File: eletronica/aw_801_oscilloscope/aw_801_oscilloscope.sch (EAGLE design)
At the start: 54 parts, among them IC1 ICL7660CPA, IC3 MEGA8-P, IC4 LM4558N, Q2 16Mhz, X1 ANALOG, X2 USB, X3 DIG

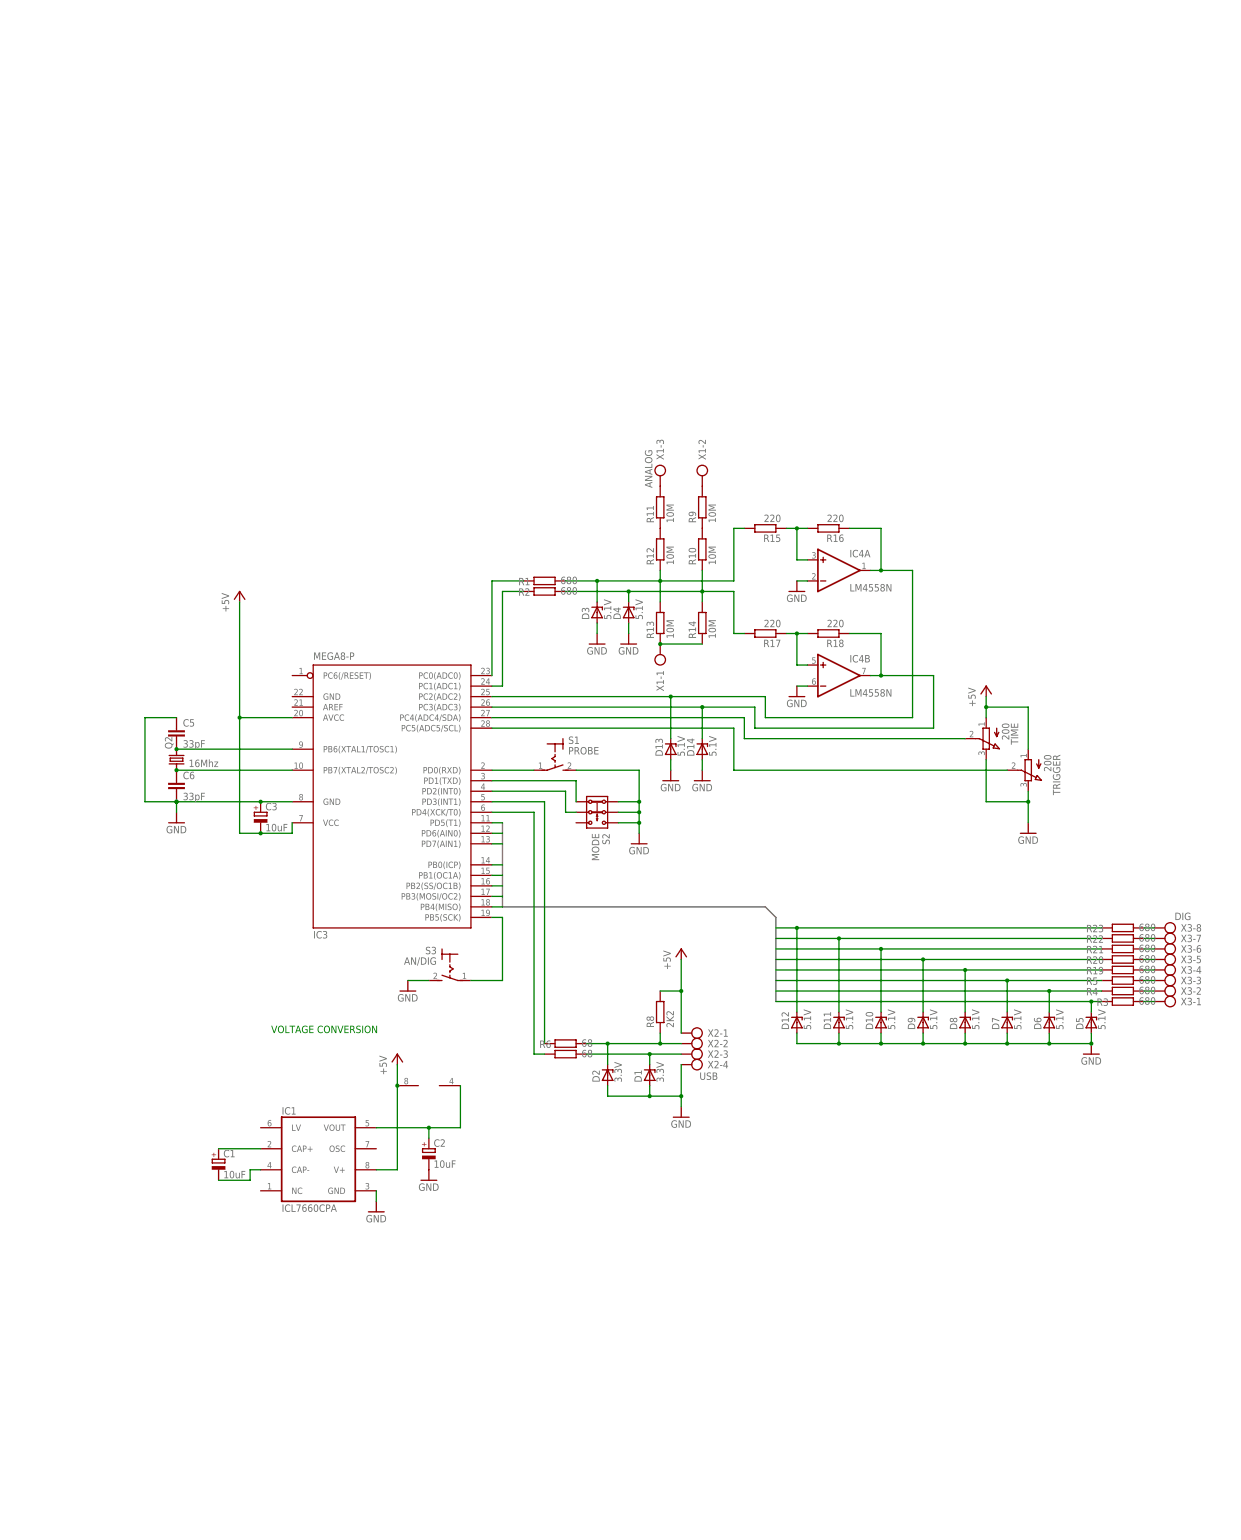
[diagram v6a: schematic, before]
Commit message: 
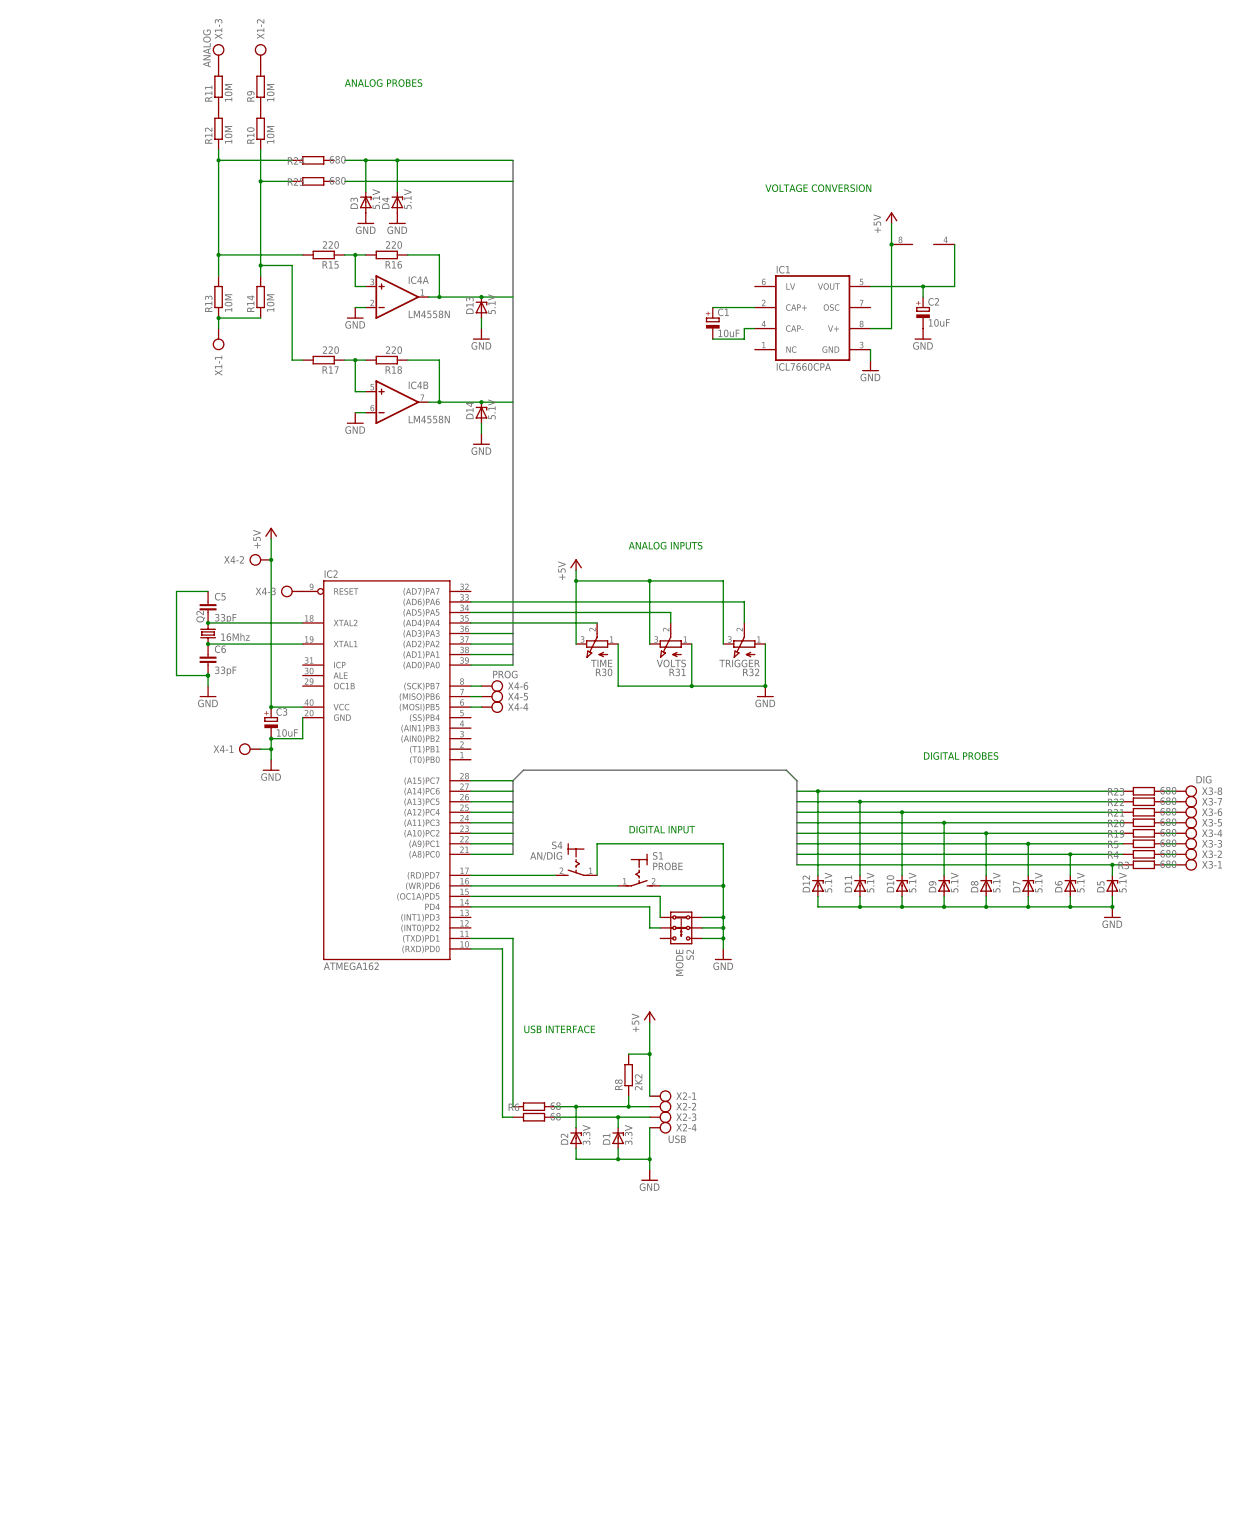
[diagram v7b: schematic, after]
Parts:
- removed IC3: MEGA8-P, atmel:MEGA8-P
- removed R1, R2: 680, rcl:R-EU_0207/10
- removed S3: AN/DIG, switch:MS243
- removed TIME, TRIGGER: 200, pot:3RP/1610N
- added IC2: ATMEGA162, atmel:AT90S8515P
- added R24, R25: 680, rcl:R-EU_0207/10
- added R30: TIME, pot:3RP/1610N
- added R31: VOLTS, pot:3RP/1610N
- added R32: TRIGGER, pot:3RP/1610N
- added S4: AN/DIG, switch:MS243
- added X4: PROG, con-ptr500:AK300/6
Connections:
- removed net N$35: IC3.PB5(SCK), S3.P
- new net ANALOG0: D3.C, D4.C, IC2.(AD0)PA0
- new net ANALOG1: IC2.(AD1)PA1
- new net ANALOG2: D13.C, IC2.(AD2)PA2, IC4A.OUT, R16.1
- new net ANALOG3: D14.C, IC2.(AD3)PA3, IC4B.OUT, R18.1
- new net N$36: IC2.(WR)PD6, S1.P
- new net N$37: IC2.(TXD)PD1, R6.1
- net +5V: now also C3.+, IC2.VCC, R30.E, R31.E, R32.E, X4-2.KL; no longer C3.-, IC3.AVCC, IC3.VCC@1, TIME.A, TRIGGER.A
- net DIG0: now also IC2.(A8)PC0; no longer IC3.PD5(T1)
- net DIG1: now also IC2.(A9)PC1; no longer IC3.PD6(AIN0)
- net DIG2: now also IC2.(A10)PC2; no longer IC3.PD7(AIN1)
- net DIG3: now also IC2.(A11)PC3; no longer IC3.PB0(ICP)
- net DIG4: now also IC2.(A12)PC4; no longer IC3.PB1(OC1A)
- net DIG5: now also IC2.(A13)PC5; no longer IC3.PB2(SS/OC1B)
- net DIG6: now also IC2.(A14)PC6; no longer IC3.PB3(MOSI/OC2)
- net DIG7: now also IC2.(A15)PC7; no longer IC3.PB4(MISO)
- net GND: now also C3.-, IC2.GND, R30.A, R31.A, R32.A, S4.P, X4-1.KL; no longer C3.+, IC3.GND@1, S3.S, TIME.E, TRIGGER.E
- net N$1: now also R24.1; no longer D3.C, R1.2
- net N$11: now also IC2.(SCK)PB7, X4-6.KL; no longer IC3.PD3(INT1), R6.1
- net N$12: now also IC2.(RXD)PD0; no longer IC3.PD4(XCK/T0)
- net N$16: now also R25.1; no longer D4.C, R2.2
- net N$18: now also IC2.(AD5)PA5, R31.S; no longer D13.C, IC3.PC2(ADC2), IC4A.OUT, R16.1
- net N$20: now also IC2.(AD6)PA6, R32.S; no longer D14.C, IC3.PC3(ADC3), IC4B.OUT, R18.1
- net N$22: now also IC2.(MISO)PB6, X4-5.KL; no longer IC3.PC4(ADC4/SDA), TIME.S
- net N$23: now also IC2.(MOSI)PB5, X4-4.KL; no longer IC3.PC5(ADC5/SCL), TRIGGER.S
- net N$33: now also IC2.RESET, X4-3.KL; no longer IC3.PC1(ADC1), R2.1
- net N$34: now also IC2.(RD)PD7, S4.S; no longer IC3.PC0(ADC0), R1.1
- net N$4: now also IC2.(AD4)PA4, R30.S; no longer IC3.PD0(RXD), S1.P
- net N$5: now also IC2.(OC1A)PD5; no longer IC3.PD1(TXD)
- net N$6: now also IC2.PD4; no longer IC3.PD2(INT0)
- net N$7: now also IC2.XTAL2; no longer IC3.PB6(XTAL1/TOSC1)
- net N$8: now also IC2.XTAL1; no longer IC3.PB7(XTAL2/TOSC2)
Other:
- note added: "ANALOG INPUTS"
- note added: "ANALOG PROBES"
- note added: "DIGITAL INPUT"
- note added: "DIGITAL PROBES"
- note added: "USB INTERFACE"
- moved on the sheet: C1, C2, C3, C5, C6, D1, D10, D11, D12, D13, D14, D2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

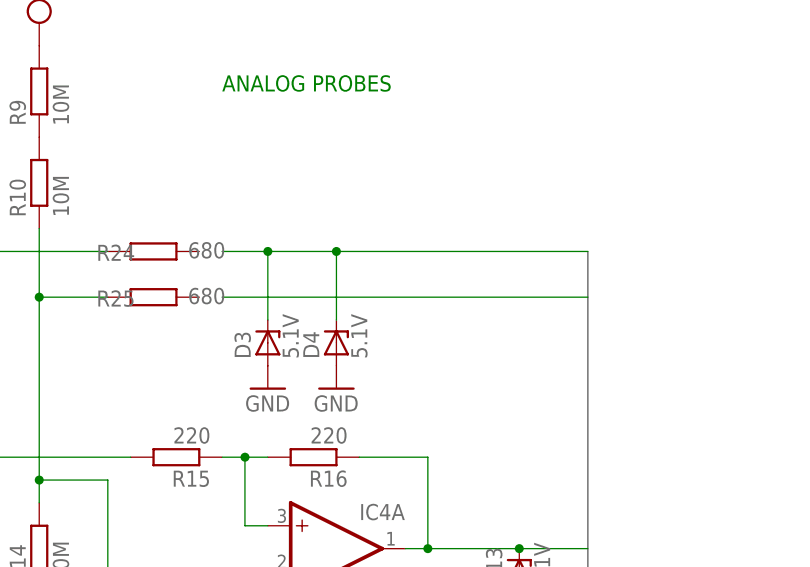
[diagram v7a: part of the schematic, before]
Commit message: 
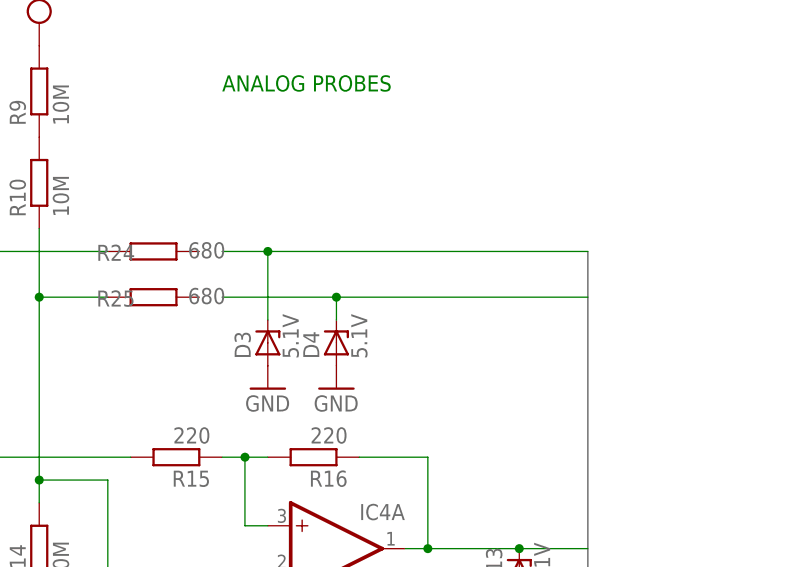
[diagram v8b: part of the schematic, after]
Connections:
- net ANALOG0: no longer D4.C
- net ANALOG1: now also D4.C
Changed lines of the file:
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@@
 <wire x1="66.04" y1="264.16" x2="71.12" y2="264.16" width="0.1524" layer="91"/>
 <pinref part="D3" gate="G$1" pin="C"/>
-<wire x1="71.12" y1="264.16" x2="78.74" y2="264.16" width="0.1524" layer="91"/>
 <wire x1="71.12" y1="264.16" x2="71.12" y2="256.54" width="0.1524" layer="91"/>
 <junction x="71.12" y="264.16"/>
-<pinref part="D4" gate="G$1" pin="C"/>
-<wire x1="78.74" y1="264.16" x2="78.74" y2="256.54" width="0.1524" layer="91"/>
-<junction x="78.74" y="264.16"/>
-<wire x1="106.68" y1="264.16" x2="78.74" y2="264.16" width="0.1524" layer="91"/>
+<wire x1="106.68" y1="264.16" x2="71.12" y2="264.16" width="0.1524" layer="91"/>
 </segment>
 <segment>
@@
 <net name="ANALOG1" class="0">
 <segment>
-<wire x1="106.68" y1="259.08" x2="66.04" y2="259.08" width="0.1524" layer="91"/>
+<wire x1="106.68" y1="259.08" x2="78.74" y2="259.08" width="0.1524" layer="91"/>
+<pinref part="D4" gate="G$1" pin="C"/>
+<wire x1="78.74" y1="259.08" x2="66.04" y2="259.08" width="0.1524" layer="91"/>
+<wire x1="78.74" y1="256.54" x2="78.74" y2="259.08" width="0.1524" layer="91"/>
+<junction x="78.74" y="259.08"/>
 </segment>
 <segment>
